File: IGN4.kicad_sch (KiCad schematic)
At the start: 16 parts, among them Q1 ISL9V3040D3ST, Q2 ISL9V3040D3ST, Q3 ISL9V3040D3ST, Q4 ISL9V3040D3ST

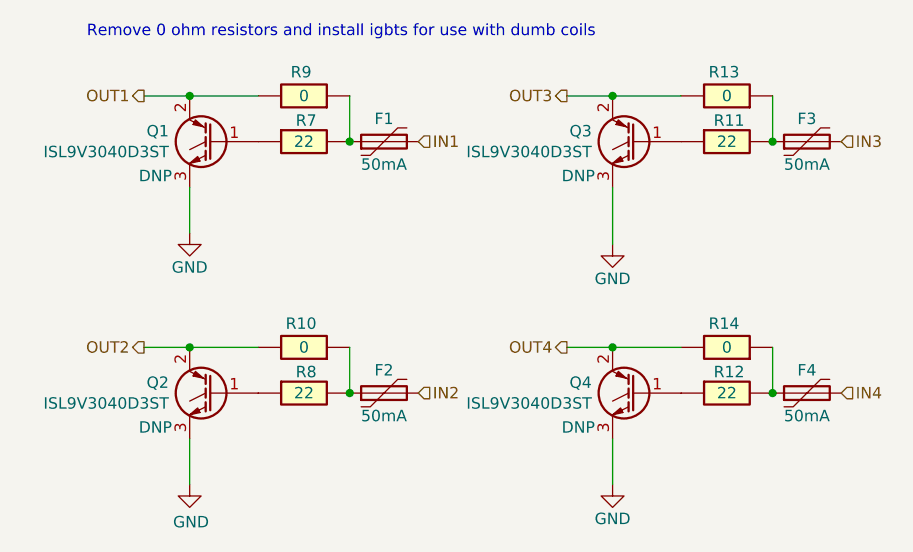
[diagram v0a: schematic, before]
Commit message: add submodules for ign and inj + flyback protected output
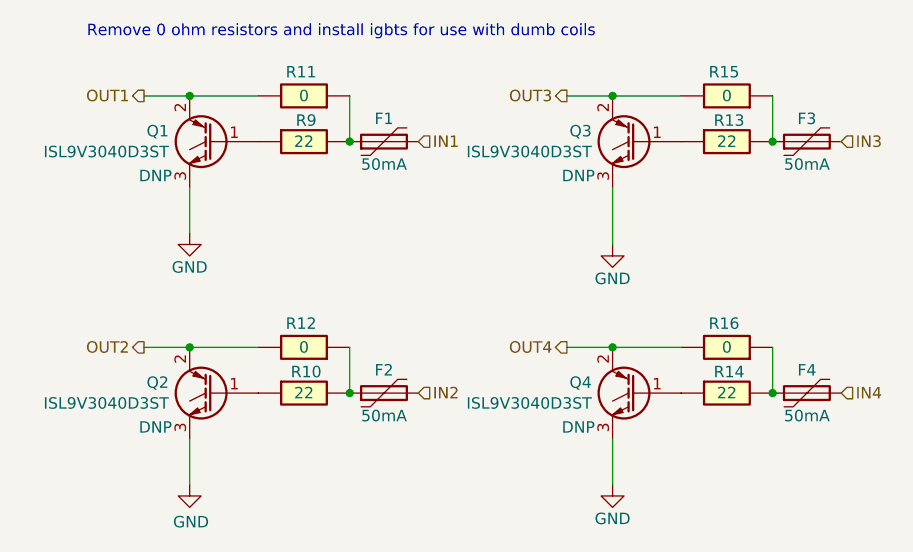
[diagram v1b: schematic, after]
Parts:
- R10: renamed from R8; footprint hellen-one-common:R0603 -> footprints:R0603
- R13: renamed from R11; footprint hellen-one-common:R0603 -> footprints:R0603
- R14: renamed from R12; footprint hellen-one-common:R0603 -> footprints:R0603
- R9: renamed from R7; footprint hellen-one-common:R0603 -> footprints:R0603
- renumbered R9 to R11, R10 to R12, R13 to R15, R14 to R16
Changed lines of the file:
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@@
 		(on_board yes)
 		(dnp no)
-		(property "Reference" "R12"
+		(property "Reference" "R14"
 			(at 185.662 103.0618 0)
 			(effects
@@
 			)
 		)
-		(property "Footprint" "hellen-one-common:R0603"
+		(property "Footprint" "footprints:R0603"
 			(at 184.15 101.6 0)
 			(effects
@@
 			(project "EP91Starlet"
 				(path "/10fbc709-889c-4565-8161-129ca9f0b73f/06db1531-b20e-49b5-8793-6d74da2374bc"
-					(reference "R12")
+					(reference "R14")
 					(unit 1)
 				)
@@
 		(on_board yes)
 		(dnp no)
-		(property "Reference" "#PWR8"
+		(property "Reference" "#PWR19"
 			(at 172.72 95.25 0)
 			(effects
@@
 			(project "EP91Starlet"
 				(path "/10fbc709-889c-4565-8161-129ca9f0b73f/06db1531-b20e-49b5-8793-6d74da2374bc"
-					(reference "#PWR8")
+					(reference "#PWR19")
 					(unit 1)
 				)
@@
 		(on_board yes)
 		(dnp no)
-		(property "Reference" "#PWR9"
+		(property "Reference" "#PWR20"
 			(at 172.72 121.92 0)
 			(effects
@@
 			(project "EP91Starlet"
 				(path "/10fbc709-889c-4565-8161-129ca9f0b73f/06db1531-b20e-49b5-8793-6d74da2374bc"
-					(reference "#PWR9")
+					(reference "#PWR20")
 					(unit 1)
 				)
@@
 		(on_board yes)
 		(dnp no)
-		(property "Reference" "#PWR6"
+		(property "Reference" "#PWR17"
 			(at 125.73 93.98 0)
 			(effects
@@
 			(project "EP91Starlet"
 				(path "/10fbc709-889c-4565-8161-129ca9f0b73f/06db1531-b20e-49b5-8793-6d74da2374bc"
-					(reference "#PWR6")
+					(reference "#PWR17")
 					(unit 1)
 				)
@@
 		(on_board yes)
 		(dnp no)
-		(property "Reference" "R9"
+		(property "Reference" "R11"
 			(at 138.1096 69.7453 0)
 			(effects
@@
 			(project "EP91Starlet"
 				(path "/10fbc709-889c-4565-8161-129ca9f0b73f/06db1531-b20e-49b5-8793-6d74da2374bc"
-					(reference "R9")
+					(reference "R11")
 					(unit 1)
 				)
@@
 		(on_board yes)
 		(dnp no)
-		(property "Reference" "R11"
+		(property "Reference" "R13"
 			(at 185.662 75.1218 0)
 			(effects
@@
 			)
 		)
-		(property "Footprint" "hellen-one-common:R0603"
+		(property "Footprint" "footprints:R0603"
 			(at 184.15 73.66 0)
 			(effects
@@
 			(project "EP91Starlet"
 				(path "/10fbc709-889c-4565-8161-129ca9f0b73f/06db1531-b20e-49b5-8793-6d74da2374bc"
-					(reference "R11")
+					(reference "R13")
 					(unit 1)
 				)
@@
 		(on_board yes)
 		(dnp no)
-		(property "Reference" "R14"
+		(property "Reference" "R16"
 			(at 185.0996 97.6853 0)
 			(effects
@@
 			(project "EP91Starlet"
 				(path "/10fbc709-889c-4565-8161-129ca9f0b73f/06db1531-b20e-49b5-8793-6d74da2374bc"
-					(reference "R14")
+					(reference "R16")
 					(unit 1)
 				)
@@
 		(on_board yes)
 		(dnp no)
-		(property "Reference" "R10"
+		(property "Reference" "R12"
 			(at 138.1096 97.6853 0)
 			(effects
@@
 			(project "EP91Starlet"
 				(path "/10fbc709-889c-4565-8161-129ca9f0b73f/06db1531-b20e-49b5-8793-6d74da2374bc"
-					(reference "R10")
+					(reference "R12")
 					(unit 1)
 				)
@@
 		(on_board yes)
 		(dnp no)
-		(property "Reference" "R7"
+		(property "Reference" "R9"
 			(at 138.672 75.1218 0)
 			(effects
@@
 			)
 		)
-		(property "Footprint" "hellen-one-common:R0603"
+		(property "Footprint" "footprints:R0603"
 			(at 137.16 73.66 0)
 			(effects
@@
 			(project "EP91Starlet"
 				(path "/10fbc709-889c-4565-8161-129ca9f0b73f/06db1531-b20e-49b5-8793-6d74da2374bc"
-					(reference "R7")
+					(reference "R9")
 					(unit 1)
 				)
@@
 		(on_board yes)
 		(dnp no)
-		(property "Reference" "R8"
+		(property "Reference" "R10"
 			(at 138.672 103.0618 0)
 			(effects
@@
 			)
 		)
-		(property "Footprint" "hellen-one-common:R0603"
+		(property "Footprint" "footprints:R0603"
 			(at 137.16 101.6 0)
 			(effects
@@
 			(project "EP91Starlet"
 				(path "/10fbc709-889c-4565-8161-129ca9f0b73f/06db1531-b20e-49b5-8793-6d74da2374bc"
-					(reference "R8")
+					(reference "R10")
 					(unit 1)
 				)
@@
 		(on_board yes)
 		(dnp no)
-		(property "Reference" "#PWR7"
+		(property "Reference" "#PWR18"
 			(at 125.73 121.92 0)
 			(effects
@@
 			(project "EP91Starlet"
 				(path "/10fbc709-889c-4565-8161-129ca9f0b73f/06db1531-b20e-49b5-8793-6d74da2374bc"
-					(reference "#PWR7")
+					(reference "#PWR18")
 					(unit 1)
 				)
@@
 		(on_board yes)
 		(dnp no)
-		(property "Reference" "R13"
+		(property "Reference" "R15"
 			(at 185.0996 69.7453 0)
 			(effects
@@
 			(project "EP91Starlet"
 				(path "/10fbc709-889c-4565-8161-129ca9f0b73f/06db1531-b20e-49b5-8793-6d74da2374bc"
-					(reference "R13")
-					(unit 1)
-				)
+					(reference "R15")
+					(unit 1)
+				)
